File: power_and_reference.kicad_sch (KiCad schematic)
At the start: 12 parts, among them Q1 ZXTN4004KQTC, U1 BQ79616PAPRQ1

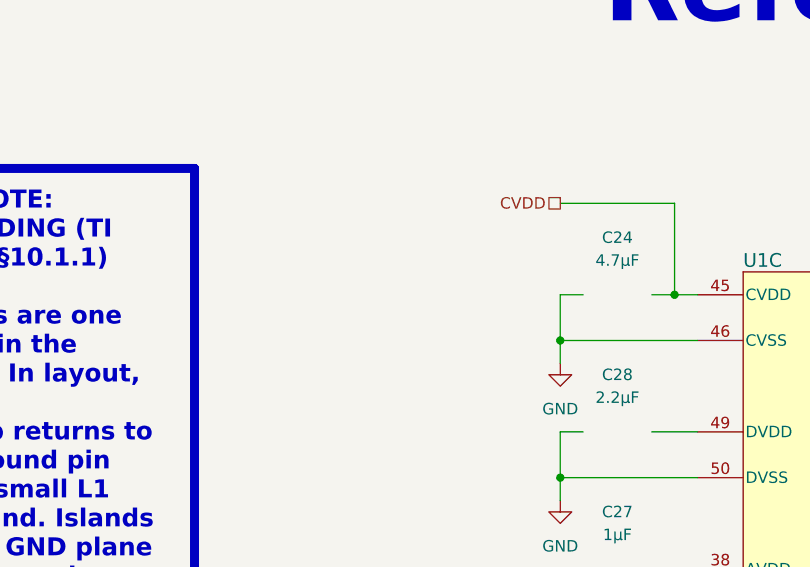
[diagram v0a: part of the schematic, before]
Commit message: SCH:[Hiarchy, Temp, Power]:Inital schmatics of temp, balance, power mostly there need to add design notes and layout notes.
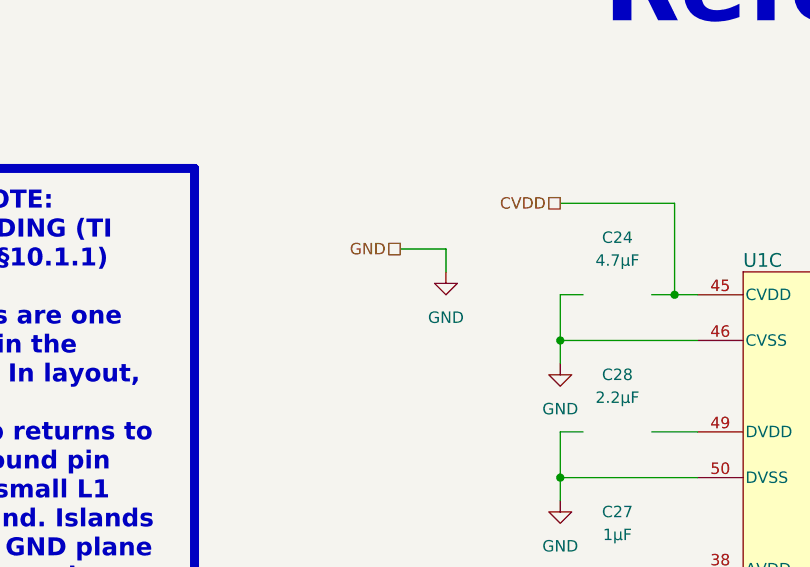
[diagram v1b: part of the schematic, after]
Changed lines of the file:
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@@
+	(wire
+		(pts
+			(xy 93.98 58.42) (xy 93.98 60.96)
+		)
+		(stroke
+			(width 0)
+			(type default)
+		)
+	)
 	(wire
 		(pts
@@
 		(pts
 			(xy 187.96 60.96) (xy 187.96 63.5)
+		)
+		(stroke
+			(width 0)
+			(type default)
+		)
+	)
+	(wire
+		(pts
+			(xy 88.9 58.42) (xy 93.98 58.42)
 		)
 		(stroke
@@
 			)
 			(justify left)
+		)
+	)
+	(hierarchical_label "GND"
+		(shape passive)
+		(at 88.9 58.42 180)
+		(effects
+			(font
+				(size 1.27 1.27)
+			)
+			(justify right)
 		)
 	)
@@
 					(unit 1)
 				)
+			)
+		)
+	)
+	(symbol
+		(lib_id "power:GND")
+		(at 93.98 60.96 0)
+		(unit 1)
+		(body_style 1)
+		(exclude_from_sim no)
+		(in_bom yes)
+		(on_board yes)
+		(in_pos_files yes)
+		(dnp no)
+		(fields_autoplaced yes)
+		(property "Reference" "#PWR015"
+			(at 93.98 67.31 0)
+			(hide yes)
+			(show_name no)
+			(do_not_autoplace no)
+			(effects
+				(font
+					(size 1.27 1.27)
+				)
+			)
+		)
+		(property "Value" "GND"
+			(at 93.98 66.04 0)
+			(show_name no)
+			(do_not_autoplace no)
+			(effects
+				(font
+					(size 1.27 1.27)
+				)
+			)
+		)
+		(property "Footprint" ""
+			(at 93.98 60.96 0)
+			(hide yes)
+			(show_name no)
+			(do_not_autoplace no)
+			(effects
+				(font
+					(size 1.27 1.27)
+				)
+			)
+		)
+		(property "Datasheet" ""
+			(at 93.98 60.96 0)
+			(hide yes)
+			(show_name no)
+			(do_not_autoplace no)
+			(effects
+				(font
+					(size 1.27 1.27)
+				)
+			)
+		)
+		(property "Description" "Power symbol creates a local label with name \"GND\" , ground"
+			(at 93.98 60.96 0)
+			(hide yes)
+			(show_name no)
+			(do_not_autoplace no)
+			(effects
+				(font
+					(size 1.27 1.27)
+				)
+			)
+		)
+		(pin "1"
+		)
+		(instances
+			(project "bms_slave"
+				(path "/f9e05184-c88b-4a88-ae9c-ab2bdb32be7c/c5103ceb-5325-4a84-a025-9638a412984e/dc8544ca-af63-40ad-8cbc-696b729b5531"
+					(reference "#PWR015")
+					(unit 1)
+				)

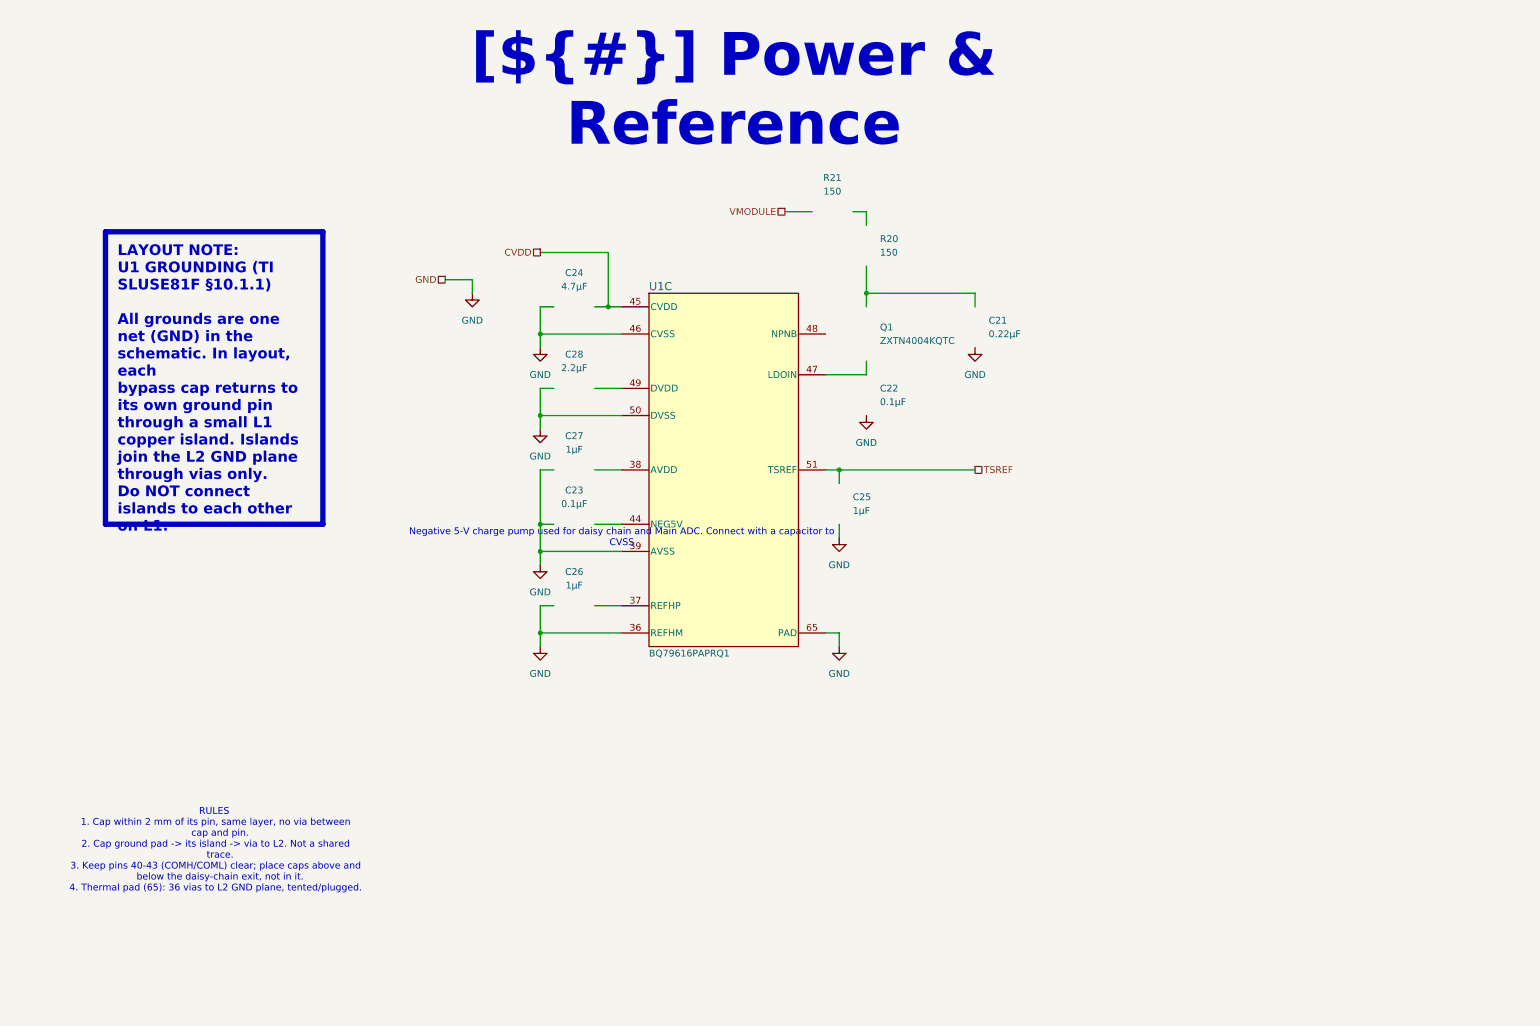
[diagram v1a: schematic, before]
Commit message: SCH: Schmatic is close to final, need to resolve a few ERC errors nothing major. Largest change will be adding seporate wires for VBAT and RefGround / Tap 0. connector position and types may change as mechaincal posision/layout is finalaized as well so holding off on layout for now.
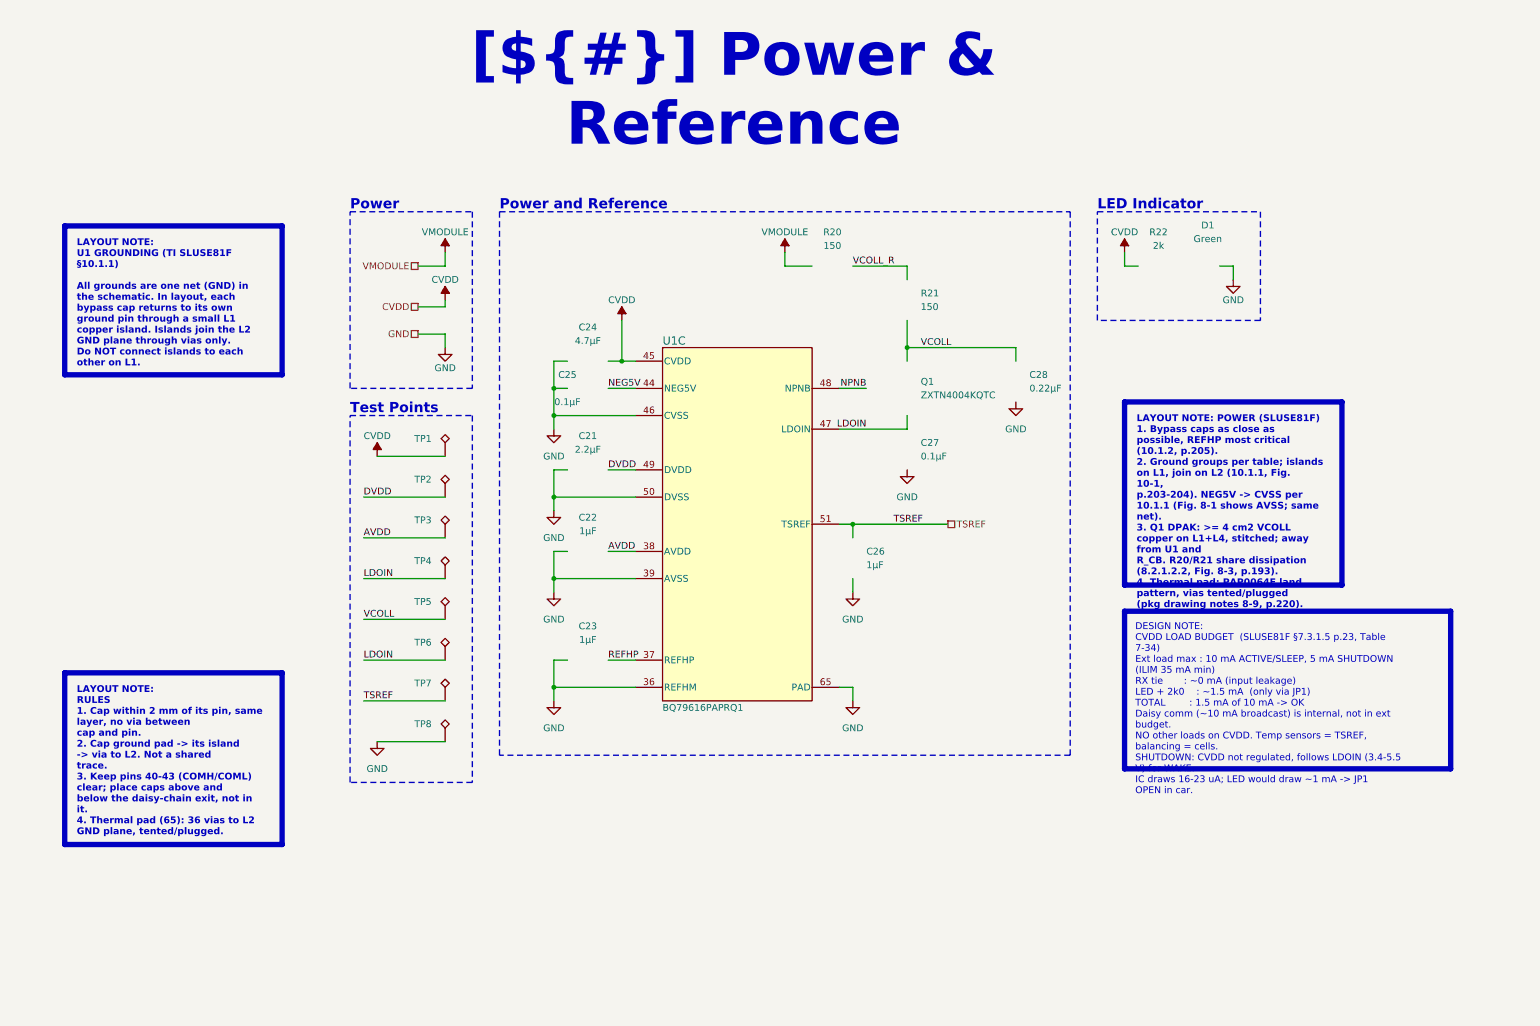
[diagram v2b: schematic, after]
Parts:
- removed C23: 0.1µF, remote_cl05a105ko5nnnc:C_0402_1005Metric, symbol remote_gcm155r71h104ke02j:C
- added C25: 0.1µF, remote_cl05a105ko5nnnc:C_0402_1005Metric, symbol remote_gcm155r71h104ke02j:C
- added D1: Green, remote_ltst-c190tbkt:LED_0603_1608Metric, symbol remote_ltst-c190kgkt:LED
- added R22: 2k, remote_erj-2ge0r00x:R_0402_1005Metric, symbol remote_era-2apb202x:RT0402BRD0710KL
- added TP1, TP2, TP3, TP4, TP5, TP6, TP7, TP8: (no value), TestPoint:TestPoint_Pad_D2.0mm, symbol Connector:TestPoint_Alt
- renumbered C28 to C21, C27 to C22, C26 to C23, C25 to C26, C22 to C27, C21 to C28, R21 to R20, R20 to R21
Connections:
- net CVDD: now also R22.1, TP1.1
- net GND: now also C25.2, D1.1 (K), TP8.1
- net TSREF: now also TP7.1
- net VCOLL: now reaches C28.1, Q1.1 (C), R21.2
- net VCOLL: now also TP5.1
- net NPNB: now reaches Q1.2 (B), U1.48 (NPNB)
- net LDOIN: now reaches C27.2, Q1.3 (E), U1.47 (LDOIN)
- net LDOIN: now also TP4.1, TP6.1
- net REFHP: now reaches C23.2, U1.37 (REFHP)
- net AVDD: now reaches C22.2, U1.38 (AVDD)
- net AVDD: now also TP3.1
- net NEG5V: now reaches U1.44 (NEG5V)
- net NEG5V: now also C25.1
- net DVDD: now reaches C21.2, U1.49 (DVDD)
- net DVDD: now also TP2.1
- net VCOLL_R: now reaches R20.2, R21.1
- new net: D1.2 (A), R22.2
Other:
- note added: "LED Indicator"
- note added: "Power"
- note added: "Power and Reference"
- note added: "Test Points"
- note removed: "Negative 5-V charge pump used for daisy chain and Main ADC. Connect with a capacitor to CVSS"
- note removed: "RULES 1. Cap within 2 mm of its pin, same layer, no via between cap and pin. 2. Cap ground pad -> its island -> via to L2. Not a shared trace. 3. Keep pins 40-43 (COMH/COML) clear; place caps above and below the daisy-chain exit, not in it. 4. Thermal pad (65): 36 vias to L2 GND plane, tented/plugged."

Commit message: SCH[Cleaning]:Updated Connectors not sure still, added sprate bat and ground connections, updated commincation conncetors. PCB[Layout]:Inital layout of compents need to fit on board size once tap connecton method is decided.
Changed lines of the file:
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@@
 	)
 	(symbol
-		(lib_id "remote_zxtn4004kqtc:NPN")
-		(at 167.64 78.74 0)
-		(unit 1)
-		(body_style 0)
-		(exclude_from_sim no)
-		(in_bom yes)
-		(on_board yes)
-		(in_pos_files yes)
-		(dnp no)
-		(fields_autoplaced yes)
-		(property "Reference" "Q1"
-			(at 177.8 77.4699 0)
-			(show_name no)
-			(do_not_autoplace no)
-			(effects
-				(font
-					(size 1.27 1.27)
-				)
-				(justify left)
-			)
-		)
-		(property "Value" "ZXTN4004KQTC"
-			(at 177.8 80.0099 0)
-			(show_name no)
-			(do_not_autoplace no)
-			(effects
-				(font
-					(size 1.27 1.27)
-				)
-				(justify left)
-			)
-		)
-		(property "Footprint" "remote_zxtn4004kqtc:DPAK_04KQTC_DIO"
-			(at 167.64 78.74 0)
-			(hide yes)
-			(show_name no)
-			(do_not_autoplace no)
-			(effects
-				(font
-					(size 1.27 1.27)
-				)
-			)
-		)
-		(property "Datasheet" "https://www.diodes.com/assets/Datasheets/ZXTN4004K.pdf"
-			(at 167.64 78.74 0)
-			(hide yes)
-			(show_name no)
-			(do_not_autoplace no)
-			(effects
-				(font
-					(size 1.27 1.27)
-				)
-			)
-		)
-		(property "Description" "Bipolar (BJT) Transistor NPN 150 V 1 A 3.8 W Surface Mount TO-252-3"
-			(at 167.64 78.74 0)
-			(hide yes)
-			(show_name no)
-			(do_not_autoplace no)
-			(effects
-				(font
-					(size 1.27 1.27)
-				)
-			)
-		)
-		(property "Manufacturer" "Diodes Incorporated"
-			(at 167.64 78.74 0)
-			(hide yes)
-			(show_name no)
-			(do_not_autoplace no)
-			(effects
-				(font
-					(size 1.27 1.27)
-				)
-			)
-		)
-		(property "Manufacturer Part Number" "ZXTN4004KQTC"
-			(at 167.64 78.74 0)
-			(hide yes)
-			(show_name no)
-			(do_not_autoplace no)
-			(effects
-				(font
-					(size 1.27 1.27)
-				)
-			)
-		)
-		(property "Vendor" ""
-			(at 167.64 78.74 0)
-			(hide yes)
-			(show_name no)
-			(do_not_autoplace no)
-			(effects
-				(font
-					(size 1.27 1.27)
-				)
-			)
-		)
-		(property "Vendor Part Number" ""
-			(at 167.64 78.74 0)
-			(hide yes)
-			(show_name no)
-			(do_not_autoplace no)
-			(effects
-				(font
-					(size 1.27 1.27)
-				)
-			)
-		)
-		(property "Mass (g)" ""
-			(at 167.64 78.74 0)
-			(hide yes)
-			(show_name no)
-			(do_not_autoplace no)
-			(effects
-				(font
-					(size 1.27 1.27)
-				)
-			)
-		)
-		(property "RQjC (C/W)" ""
-			(at 167.64 78.74 0)
-			(hide yes)
-			(show_name no)
-			(do_not_autoplace no)
-			(effects
-				(font
-					(size 1.27 1.27)
-				)
-			)
-		)
-		(property "RQjC_top (C/W)" ""
-			(at 167.64 78.74 0)
-			(hide yes)
-			(show_name no)
-			(do_not_autoplace no)
-			(effects
-				(font
-					(size 1.27 1.27)
-				)
-			)
-		)
-		(property "Temp_max (C)" ""
-			(at 167.64 78.74 0)
-			(hide yes)
-			(show_name no)
-			(do_not_autoplace no)
-			(effects
-				(font
-					(size 1.27 1.27)
-				)
-			)
-		)
-		(property "Temp_min (C)" ""
-			(at 167.64 78.74 0)
-			(hide yes)
-			(show_name no)
-			(do_not_autoplace no)
-			(effects
-				(font
-					(size 1.27 1.27)
-				)
-			)
-		)
-		(property "Power Dissipation (W)" ""
-			(at 167.64 78.74 0)
-			(hide yes)
-			(show_name no)
-			(do_not_autoplace no)
-			(effects
-				(font
-					(size 1.27 1.27)
-				)
-			)
-		)
-		(property "Rate" ""
-			(at 167.64 78.74 0)
-			(hide yes)
-			(show_name no)
-			(do_not_autoplace no)
-			(effects
-				(font
-					(size 1.27 1.27)
-				)
-			)
-		)
-		(property "SAP Code" ""
-			(at 167.64 78.74 0)
-			(hide yes)
-			(show_name no)
-			(do_not_autoplace no)
-			(effects
-				(font
-					(size 1.27 1.27)
-				)
-			)
-		)
-		(pin "2"
-		)
-		(pin "3"
-		)
-		(pin "1"
-		)
-		(instances
-			(project "bms_slave"
-				(path "/f9e05184-c88b-4a88-ae9c-ab2bdb32be7c/c5103ceb-5325-4a84-a025-9638a412984e/dc8544ca-af63-40ad-8cbc-696b729b5531"
-					(reference "Q1")
-					(unit 1)
-				)
-			)
-		)
-	)
-	(symbol
 		(lib_id "power:GND")
 		(at 109.22 86.36 0)
@@
 					(unit 1)
 				)
+			)
+		)
+	)
+	(symbol
+		(lib_id "remote_zxtn4004kqtc:NPN")
+		(at 167.64 78.74 0)
+		(unit 1)
+		(body_style 0)
+		(exclude_from_sim no)
+		(in_bom yes)
+		(on_board yes)
+		(in_pos_files yes)
+		(dnp no)
+		(fields_autoplaced yes)
+		(property "Reference" "Q1"
+			(at 177.8 77.47 0)
+			(show_name no)
+			(do_not_autoplace no)
+			(effects
+				(font
+					(size 1.27 1.27)
+				)
+				(justify left)
+			)
+		)
+		(property "Value" "ZXTN4004KQTC"
+			(at 177.8 80.01 0)
+			(show_name no)
+			(do_not_autoplace no)
+			(effects
+				(font
+					(size 1.27 1.27)
+				)
+				(justify left)
+			)
+		)
+		(property "Footprint" "remote_zxtn4004kqtc:DPAK_04KQTC_DIO"
+			(at 167.64 78.74 0)
+			(hide yes)
+			(show_name no)
+			(do_not_autoplace no)
+			(effects
+				(font
+					(size 1.27 1.27)
+				)
+			)
+		)
+		(property "Datasheet" "https://www.diodes.com/assets/Datasheets/ZXTN4004K.pdf"
+			(at 167.64 78.74 0)
+			(hide yes)
+			(show_name no)
+			(do_not_autoplace no)
+			(effects
+				(font
+					(size 1.27 1.27)
+				)
+			)
+		)
+		(property "Description" "Bipolar (BJT) Transistor NPN 150 V 1 A 3.8 W Surface Mount TO-252-3"
+			(at 167.64 78.74 0)
+			(hide yes)
+			(show_name no)
+			(do_not_autoplace no)
+			(effects
+				(font
+					(size 1.27 1.27)
+				)
+			)
+		)
+		(property "Manufacturer" "Diodes Incorporated"
+			(at 167.64 78.74 0)
+			(hide yes)
+			(show_name no)
+			(do_not_autoplace no)
+			(effects
+				(font
+					(size 1.27 1.27)
+				)
+			)
+		)
+		(property "Manufacturer Part Number" "ZXTN4004KQTC"
+			(at 167.64 78.74 0)
+			(hide yes)
+			(show_name no)
+			(do_not_autoplace no)
+			(effects
+				(font
+					(size 1.27 1.27)
+				)
+			)
+		)
+		(property "Vendor" ""
+			(at 167.64 78.74 0)
+			(hide yes)
+			(show_name no)
+			(do_not_autoplace no)
+			(effects
+				(font
+					(size 1.27 1.27)
+				)
+			)
+		)
+		(property "Vendor Part Number" ""
+			(at 167.64 78.74 0)
+			(hide yes)
+			(show_name no)
+			(do_not_autoplace no)
+			(effects
+				(font
+					(size 1.27 1.27)
+				)
+			)
+		)
+		(property "Mass (g)" ""
+			(at 167.64 78.74 0)
+			(hide yes)
+			(show_name no)
+			(do_not_autoplace no)
+			(effects
+				(font
+					(size 1.27 1.27)
+				)
+			)
+		)
+		(property "RQjC (C/W)" ""
+			(at 167.64 78.74 0)
+			(hide yes)
+			(show_name no)
+			(do_not_autoplace no)
+			(effects
+				(font
+					(size 1.27 1.27)
+				)
+			)
+		)
+		(property "RQjC_top (C/W)" ""
+			(at 167.64 78.74 0)
+			(hide yes)
+			(show_name no)
+			(do_not_autoplace no)
+			(effects
+				(font
+					(size 1.27 1.27)
+				)
+			)
+		)
+		(property "Temp_max (C)" ""
+			(at 167.64 78.74 0)
+			(hide yes)
+			(show_name no)
+			(do_not_autoplace no)
+			(effects
+				(font
+					(size 1.27 1.27)
+				)
+			)
+		)
+		(property "Temp_min (C)" ""
+			(at 167.64 78.74 0)
+			(hide yes)
+			(show_name no)
+			(do_not_autoplace no)
+			(effects
+				(font
+					(size 1.27 1.27)
+				)
+			)
+		)
+		(property "Power Dissipation (W)" ""
+			(at 167.64 78.74 0)
+			(hide yes)
+			(show_name no)
+			(do_not_autoplace no)
+			(effects
+				(font
+					(size 1.27 1.27)
+				)
+			)
+		)
+		(property "Rate" ""
+			(at 167.64 78.74 0)
+			(hide yes)
+			(show_name no)
+			(do_not_autoplace no)
+			(effects
+				(font
+					(size 1.27 1.27)
+				)
+			)
+		)
+		(property "SAP Code" ""
+			(at 167.64 78.74 0)
+			(hide yes)
+			(show_name no)
+			(do_not_autoplace no)
+			(effects
+				(font
+					(size 1.27 1.27)
+				)
+			)
+		)
+		(pin "2"
+		)
+		(pin "3"
+		)
+		(pin "1"
+		)
+		(instances
+			(project "bms_slave"
+				(path "/f9e05184-c88b-4a88-ae9c-ab2bdb32be7c/c5103ceb-5325-4a84-a025-9638a412984e/dc8544ca-af63-40ad-8cbc-696b729b5531"
+					(reference "Q1")
+					(unit 1)
+				)

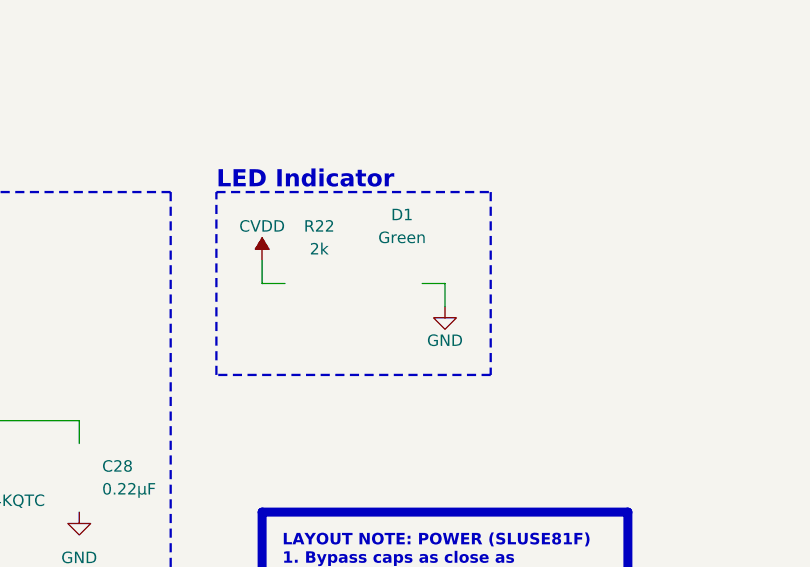
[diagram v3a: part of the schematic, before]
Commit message: PCB[Routing, Silk]: Everything but led routed, need to do via stiching, and finish adding silk screen.
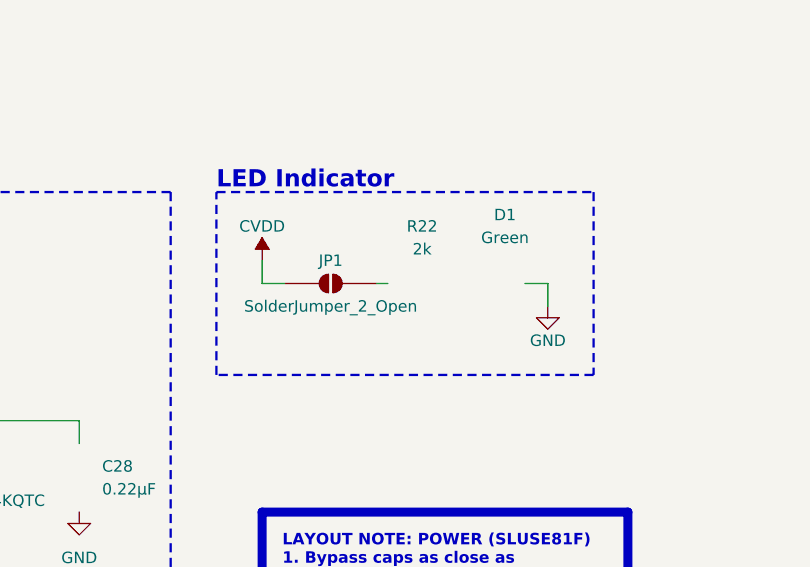
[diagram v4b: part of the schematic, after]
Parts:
- added JP1: SolderJumper_2_Open, Jumper:SolderJumper-2_P1.3mm_Open_Pad1.0x1.5mm, symbol Jumper:SolderJumper_2_Open
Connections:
- net CVDD: now also JP1.1 (A); no longer R22.1
- new net: JP1.2 (B), R22.1
